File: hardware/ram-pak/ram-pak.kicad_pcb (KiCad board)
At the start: 4 copper layers, 29 x 16.7 mm, 25 parts, among them J1 PinHeader_2x22_P1.27mm, J2 pkl_jumper, U1 TLV62568DBV, U2 W957D8MFYA5I, U3 W957D8MFYA5I

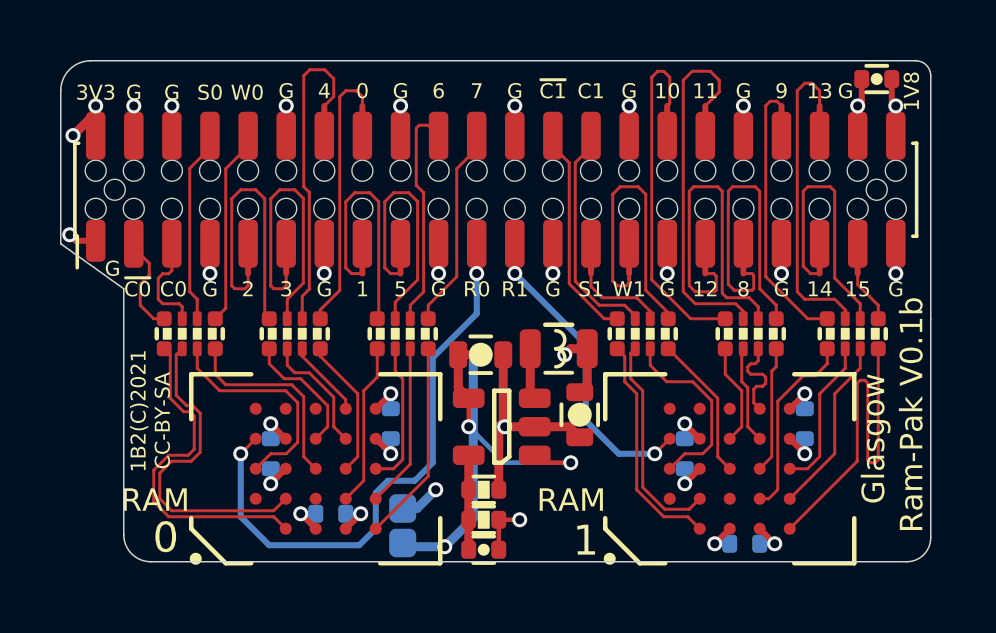
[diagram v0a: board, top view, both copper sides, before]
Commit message: ram-pak: Increased pad hole gap for improved assembly.
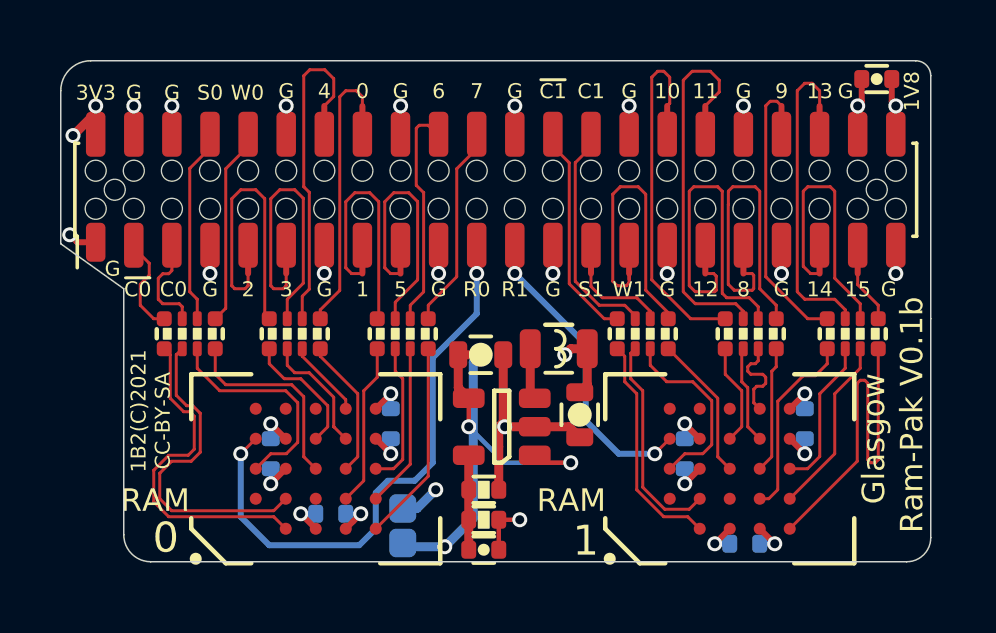
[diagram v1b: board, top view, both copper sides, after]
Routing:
- net GND: track 28.6 -> 30.7 mm
- net /DQ6x: track 8.18 -> 7.57 mm

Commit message: ram-pak: Moved some of the passives and traces from the board edge.
This should make it slightly more mechanically robust and easier to
assemble.
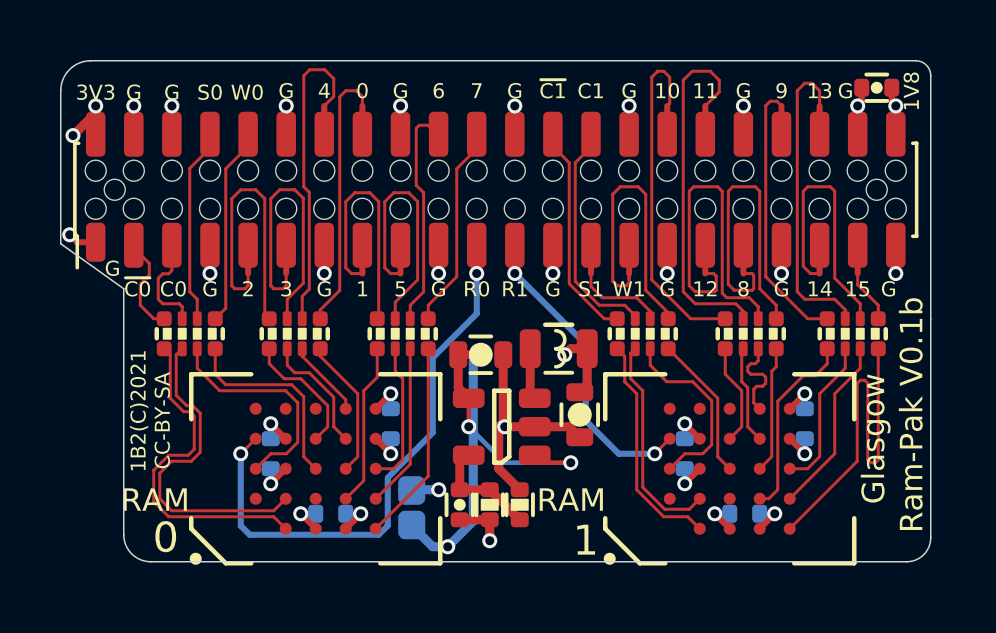
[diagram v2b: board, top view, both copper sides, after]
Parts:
- moved C3 1.70 mm to (38.8, 40.5), turned to 90 degrees
- moved R8 1.30 mm to (40.8, 40.5), turned to 90 degrees
- moved C8 1.00 mm to (48.3, 40.8)
- moved J2 0.67 mm to (37.2, 40.6)
- moved R7 0.54 mm to (39.8, 40.5), turned to 90 degrees
- moved C4 0.29 mm to (52.7, 26.6)
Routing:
- net Net-(C3-Pad2): track 3.15 -> 3.78 mm

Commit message: ram-pak: Some VREG routing cleanup.
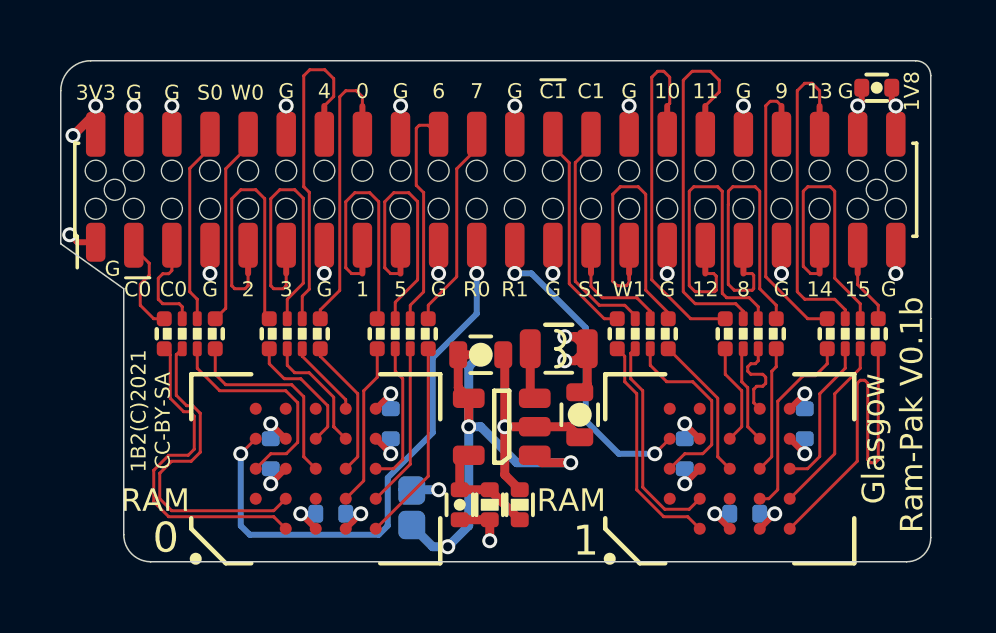
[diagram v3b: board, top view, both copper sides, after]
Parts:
- added REF**: Tab, kikit:Tab, F.Cu at (40.0, 43.7)
- added REF**: Tab, kikit:Tab, F.Cu at (40.0, 24.4)
- added REF**: Tab, kikit:Tab, F.Cu at (55.6, 29.2)
- added REF**: Tab, kikit:Tab, F.Cu at (24.5, 29.2)
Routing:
- net +1V8: track 14.2 -> 15.2 mm, vias 10 -> 11

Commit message: ram-pak: Increased hole trace spacing to 0.2mm.
To reliably manufacture the ram-pak the traces need to be at least 0.2mm
from the NPTH pin header holes. To accomplish that we had to find a
different way to lengthmatch the traces.

Bumped version to 0.1c.
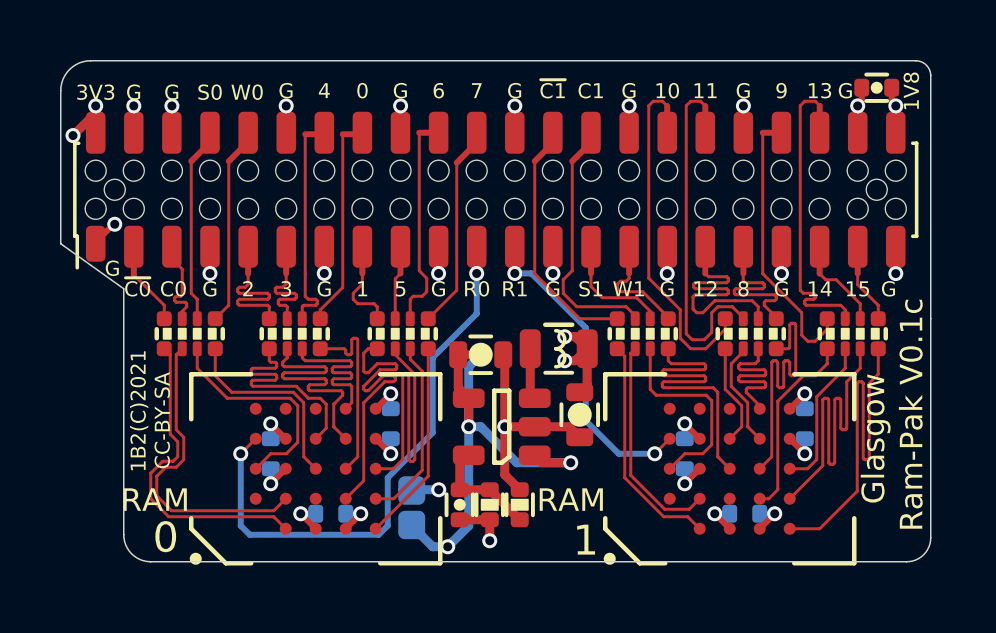
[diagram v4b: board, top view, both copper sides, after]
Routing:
- net /RWDS1x: track 11.6 -> 4.67 mm
- net /DQ5x: track 9.30 -> 2.52 mm
- net /DQ14: track 5.97 -> 12.7 mm
- net /DQ14x: track 9.87 -> 3.22 mm
- net /RWDS1: track 4.85 -> 11.2 mm
- net /DQ5: track 4.82 -> 11.1 mm
- net /DQ3x: track 10.4 -> 4.34 mm
- net /DQ1x: track 9.05 -> 3.30 mm
- net /DQ8: track 4.23 -> 9.79 mm
- net /DQ8x: track 11.5 -> 5.92 mm
- net /DQ3: track 4.09 -> 9.16 mm
- net /DQ1: track 5.43 -> 10.1 mm
- net /DQ2x: track 10.3 -> 5.68 mm
- net /DQ4x: track 11.5 -> 7.54 mm
- net /DQ2: track 4.30 -> 7.83 mm
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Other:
- board text added: "Glasgow Ram-Pak V0.1c"
- board text added: "Ram-Pak V0.1c"
- board text removed: "Glasgow Ram-Pak V0.1b"
- board text removed: "Ram-Pak V0.1b"
